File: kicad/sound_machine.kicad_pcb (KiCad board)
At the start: 2 copper layers, 75 x 45 mm, 18 parts, among them J1 Conn_01x04, J10 Conn_01x01, J11 Conn_01x01, J12 Conn_01x01, J13 Conn_01x15, J16 Conn_01x15, J2 Conn_01x15, J3 Conn_01x15, J4 Conn_01x08, J5 Audio-Jack-3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

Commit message: Labels
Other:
- board text added: "Arduino Nano"
- board text added: "USB this end"
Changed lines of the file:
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@@
     (links 76)
     (no_connects 0)
-    (area 77.150001 103.229 178.28362 162.700001)
+    (area 99.924999 104.924999 175.075001 150.075001)
     (thickness 1.6)
-    (drawings 6)
+    (drawings 8)
     (tracks 164)
     (zones 0)
@@
     (descr "Through hole straight pin header, 1x04, 2.54mm pitch, single row")
     (tags "Through hole pin header THT 1x04 2.54mm single row")
-    (fp_text reference J1 (at 0 -2.33 90) (layer F.SilkS)
+    (fp_text reference J1 (at 0 -2.33 180) (layer F.SilkS)
       (effects (font (size 1 1) (thickness 0.15)))
     )
@@
     (descr "Through hole straight pin header, 1x15, 2.54mm pitch, single row")
     (tags "Through hole pin header THT 1x15 2.54mm single row")
-    (fp_text reference J2 (at 0 -2.33) (layer F.SilkS)
+    (fp_text reference J2 (at 0 -2.33) (layer F.Fab)
       (effects (font (size 1 1) (thickness 0.15)))
     )
@@
     (descr "Through hole straight pin header, 1x15, 2.54mm pitch, single row")
     (tags "Through hole pin header THT 1x15 2.54mm single row")
-    (fp_text reference J3 (at 0 -2.33) (layer F.SilkS)
+    (fp_text reference J3 (at 0 -2.33) (layer F.Fab)
       (effects (font (size 1 1) (thickness 0.15)))
     )
@@
     (descr "DC Barrel Jack")
     (tags "Power Jack")
-    (fp_text reference J5 (at -8.45 5.75 270) (layer F.SilkS)
+    (fp_text reference J5 (at -7.04 5.75 270) (layer F.SilkS)
       (effects (font (size 1 1) (thickness 0.15)))
     )
@@
     (tags "resistor 0805")
     (attr smd)
-    (fp_text reference R1 (at 0 -1.7) (layer F.SilkS)
+    (fp_text reference R1 (at 0 1.72) (layer F.SilkS)
       (effects (font (size 1 1) (thickness 0.15)))
     )
@@
     (descr "Through hole straight pin header, 1x15, 2.54mm pitch, single row")
     (tags "Through hole pin header THT 1x15 2.54mm single row")
-    (fp_text reference J13 (at 0 -2.33) (layer F.SilkS)
+    (fp_text reference J13 (at 0 -2.33) (layer F.Fab)
       (effects (font (size 1 1) (thickness 0.15)))
     )
@@
     (descr "Through hole straight pin header, 1x15, 2.54mm pitch, single row")
     (tags "Through hole pin header THT 1x15 2.54mm single row")
-    (fp_text reference J16 (at 0 -2.33) (layer F.SilkS)
+    (fp_text reference J16 (at 0 -2.33) (layer F.Fab)
       (effects (font (size 1 1) (thickness 0.15)))
     )
@@
     (descr "Through hole straight pin header, 1x08, 2.54mm pitch, single row")
     (tags "Through hole pin header THT 1x08 2.54mm single row")
-    (fp_text reference J4 (at 0 -2.33 270) (layer F.SilkS)
+    (fp_text reference J4 (at 0 -2.33 270) (layer F.Fab)
       (effects (font (size 1 1) (thickness 0.15)))
     )
@@
     (descr "Through hole straight pin header, 1x08, 2.54mm pitch, single row")
     (tags "Through hole pin header THT 1x08 2.54mm single row")
-    (fp_text reference J6 (at 0 -2.33 270) (layer F.SilkS)
+    (fp_text reference J6 (at 0 -2.33 270) (layer F.Fab)
       (effects (font (size 1 1) (thickness 0.15)))
     )
@@
     (descr "Mounting Hole 3.2mm, M3")
     (tags "mounting hole 3.2mm m3")
-    (fp_text reference J9 (at 0 -4.2) (layer F.SilkS)
+    (fp_text reference J9 (at 0 -4.2) (layer F.Fab)
       (effects (font (size 1 1) (thickness 0.15)))
     )
@@
     (descr "Mounting Hole 3.2mm, M3")
     (tags "mounting hole 3.2mm m3")
-    (fp_text reference J10 (at 0 -4.2) (layer F.SilkS)
+    (fp_text reference J10 (at 0 -4.2) (layer F.Fab)
       (effects (font (size 1 1) (thickness 0.15)))
     )
@@
     (descr "Mounting Hole 3.2mm, M3")
     (tags "mounting hole 3.2mm m3")
-    (fp_text reference J11 (at 0 -4.2) (layer F.SilkS)
+    (fp_text reference J11 (at 0 -4.2) (layer F.Fab)
       (effects (font (size 1 1) (thickness 0.15)))
     )
@@
     (descr "Mounting Hole 3.2mm, M3")
     (tags "mounting hole 3.2mm m3")
-    (fp_text reference J12 (at 0 -4.2) (layer F.SilkS)
+    (fp_text reference J12 (at 0 -4.2) (layer F.Fab)
       (effects (font (size 1 1) (thickness 0.15)))
     )
@@
     (descr "Through hole straight pin header, 1x08, 2.54mm pitch, single row")
     (tags "Through hole pin header THT 1x08 2.54mm single row")
-    (fp_text reference U1 (at 0 -2.33) (layer F.SilkS)
+    (fp_text reference U1 (at 8.2 9.34 90) (layer F.SilkS)
       (effects (font (size 1 1) (thickness 0.15)))
     )
@@
       (effects (font (size 1 1) (thickness 0.15)))
     )
-    (fp_text user MPU-6050 (at -3 8 90) (layer F.SilkS)
+    (fp_text user MPU-6050 (at -2.4 8.04 90) (layer F.SilkS)
       (effects (font (size 1 1) (thickness 0.15)))
     )
@@
     (descr "Through hole straight socket strip, 2x08, 2.54mm pitch, double rows")
     (tags "Through hole socket strip THT 2x08 2.54mm double row")
-    (fp_text reference U2 (at 0 -2.54 270) (layer F.SilkS)
+    (fp_text reference U2 (at 0 3.82 270) (layer F.SilkS)
       (effects (font (size 1 1) (thickness 0.15)))
     )
@@
     )
   )
+  (gr_text "USB\nthis end" (at 155 143.4) (layer F.SilkS)
+    (effects (font (size 1.5 1.5) (thickness 0.3)))
+  )
+  (gr_text "Arduino\nNano" (at 155.2 128.4) (layer F.SilkS)
+    (effects (font (size 1.5 1.5) (thickness 0.3)))
+  )
   (dimension 45 (width 0.3) (layer Cmts.User)

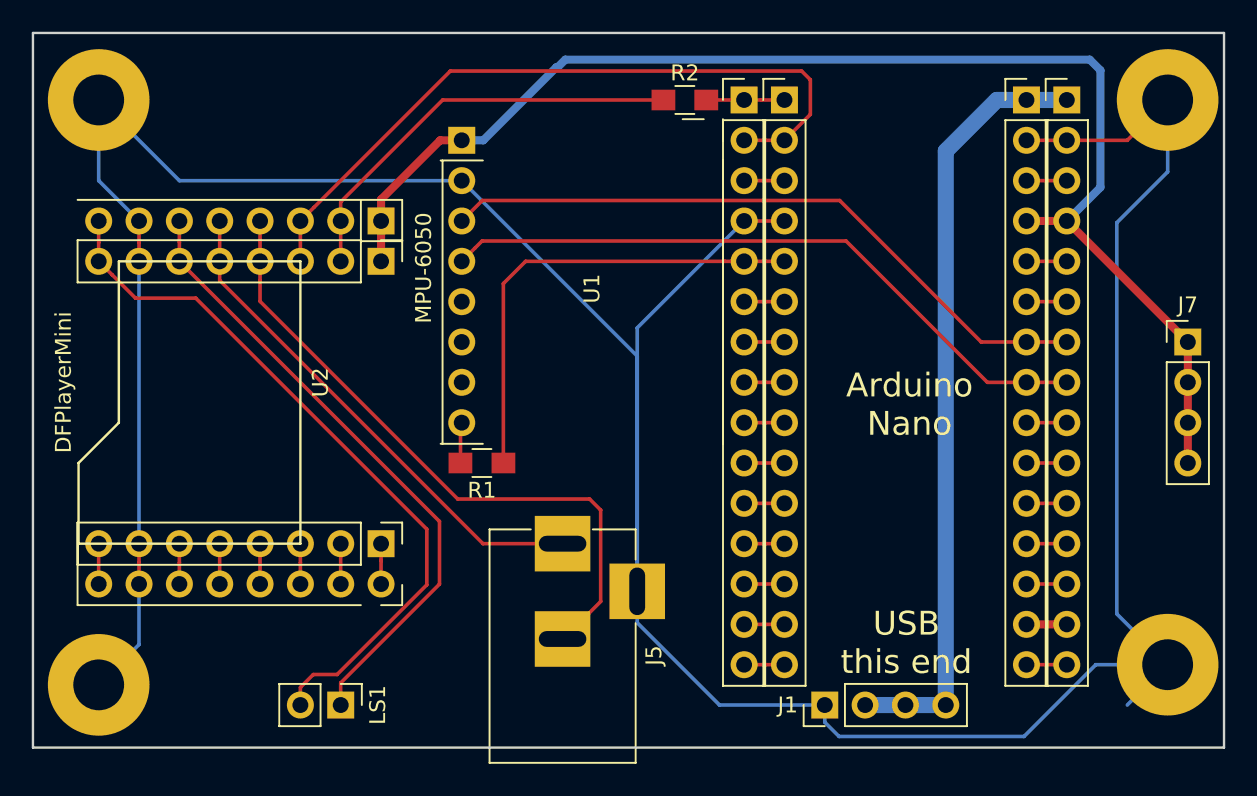
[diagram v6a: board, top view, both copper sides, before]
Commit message: Logos & labels
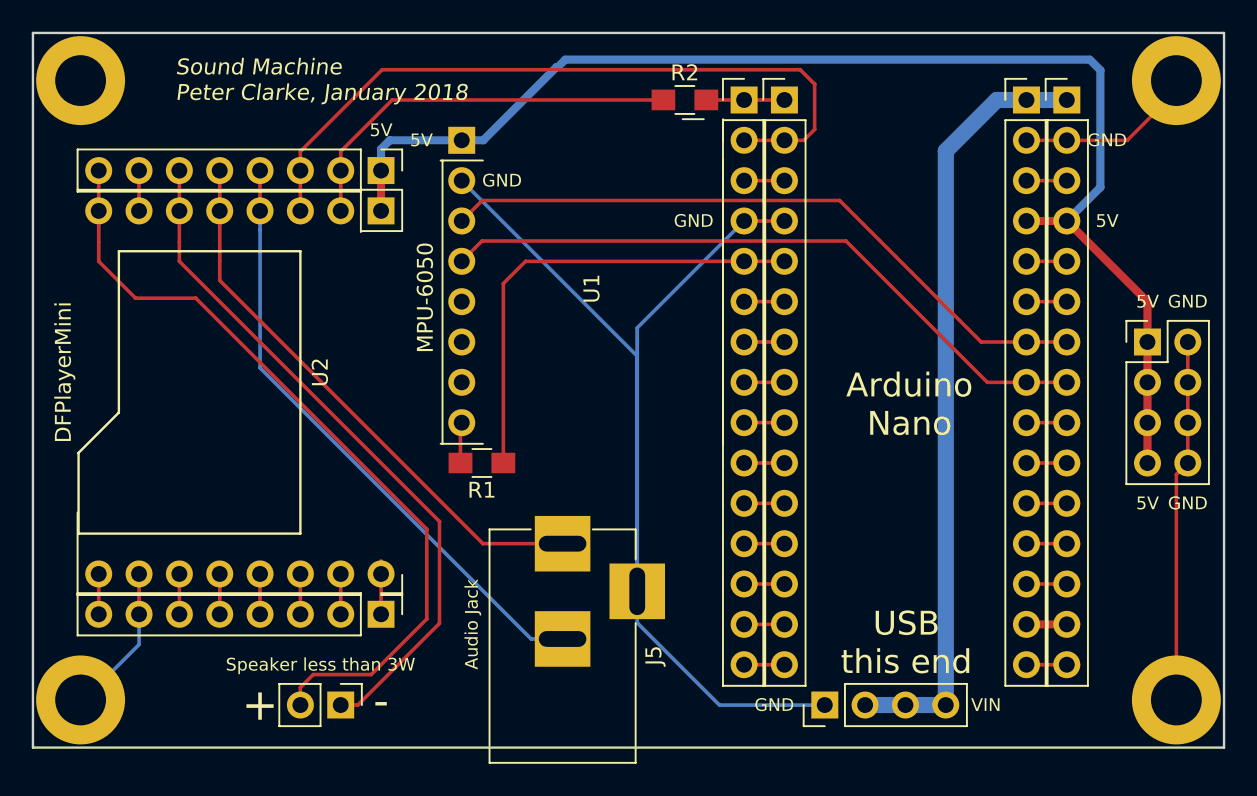
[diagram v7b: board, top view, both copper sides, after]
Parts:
- added REF**: TheApiLogoTiny, theapi:TheApiLogoTiny, F.Cu at (107.4, 105.2)
- added REF**: TheApiLogo, theapi:TheApiLogo, B.Cu at (155.7, 112.8)
- added REF**: TheApiLogoTiny, theapi:TheApiLogoTiny, B.Cu at (127.0, 131.8)
- J10, J11, J12, J9: footprint Mounting_Holes:MountingHole_3.2mm_M3_Pad -> Mounting_Holes:MountingHole_3.2mm_M3_DIN965_Pad
- J7: value Conn_01x04 -> Conn_02x04_Odd_Even; footprint Pin_Headers:Pin_Header_Straight_1x04_Pitch2.54mm -> Pin_Headers:Pin_Header_Straight_2x04_Pitch2.54mm
- moved J4 5.71 mm to (121.9, 113.7)
- moved J6 4.44 mm to (121.9, 141.6)
- moved J7 2.54 mm to (170.2, 124.5)
- moved J9 2.29 mm to (172.0, 147.0)
- moved J12 1.67 mm to (103.0, 108.0)
- moved J10 1.48 mm to (103.0, 147.0)
- moved J11 1.34 mm to (172.0, 108.0)
- moved U2 0.64 mm to (121.9, 126.4)
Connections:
- J7 pad 2: +5V -> GND
- J7 pad 4: +5V -> GND
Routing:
- net GND: track 215.6 -> 121.6 mm
- net Net-(J4-Pad8): track 45.4 -> 49.2 mm
- net Net-(J4-Pad6): track 39.8 -> 43.0 mm
- net Net-(J4-Pad5): track 32.6 -> 35.1 mm
- net Net-(J4-Pad4): track 41.1 -> 38.6 mm
- net +5V: track 84.4 -> 82.1 mm
- net Net-(J6-Pad1): track 2.54 -> 4.00 mm
- net Net-(J6-Pad6): track 2.54 -> 3.88 mm
- net Net-(J6-Pad3): track 2.54 -> 3.88 mm
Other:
- board text added: "+"
- board text added: "-"
- board text added: "5V"
- board text added: "Audio Jack"
- board text added: "GND"
- board text added: "Sound Machine Peter Clarke, January 2018"
- board text added: "Speaker less than 3W"
- board text added: "VIN"
- board text added: "https://github.com/theapi/sound_machine v1.0.0"
